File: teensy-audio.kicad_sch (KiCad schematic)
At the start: 50 parts, among them J1 AudioJack2, J10 Conn_01x05, J11 Conn_01x02, J12 Conn_01x04, J13 Conn_01x04, J2 AudioJack2, J3 Barrel_Jack, J4 Conn_02x06_Odd_Even, J5 Conn_02x08_Odd_Even, J6 Conn_02x05_Odd_Even, J7 Conn_01x04, J8 Conn_01x04, J9 Conn_02x05_Odd_Even, SW1 RotaryEncoder_Switch, SW2 SW_Push, SW3 SW_Push, SW4 SW_Push, SW5 SW_Push, U1 LM358, U2 LM7805_TO220, U3 Teensy4.0, U4 Teensy4.0_AudioShield_REVD

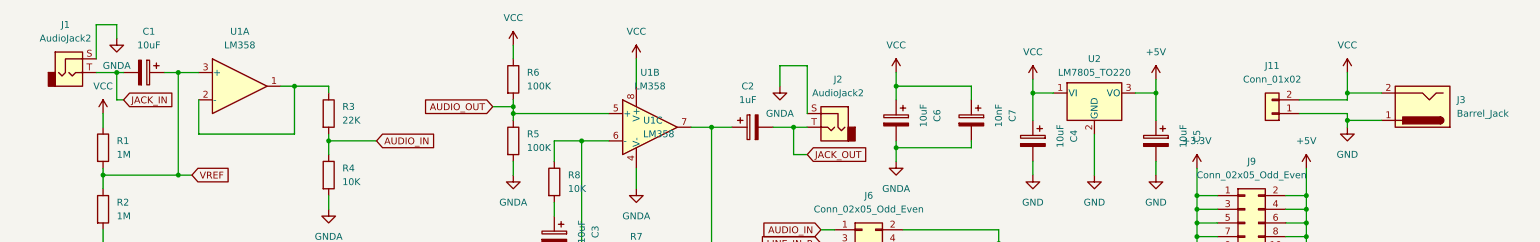
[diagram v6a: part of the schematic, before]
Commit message: corrected barrel plug
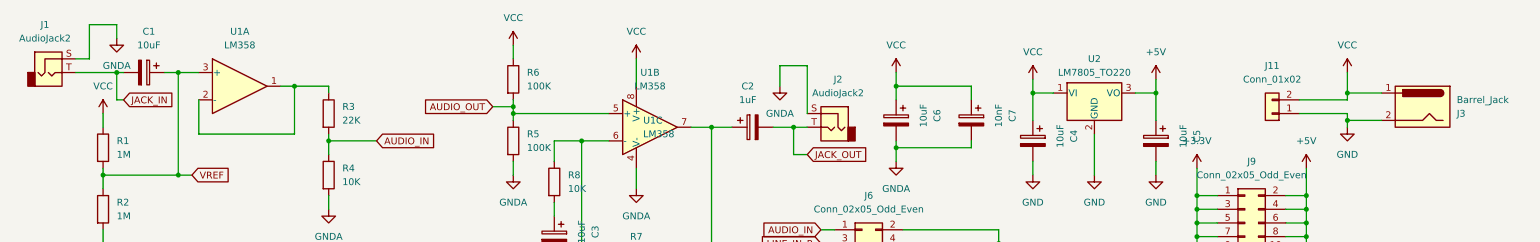
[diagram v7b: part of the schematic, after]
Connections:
- net GND: now also J3.2; no longer J3.1
- net VCC: now also J3.1; no longer J3.2
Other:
- moved on the sheet: J1, J3

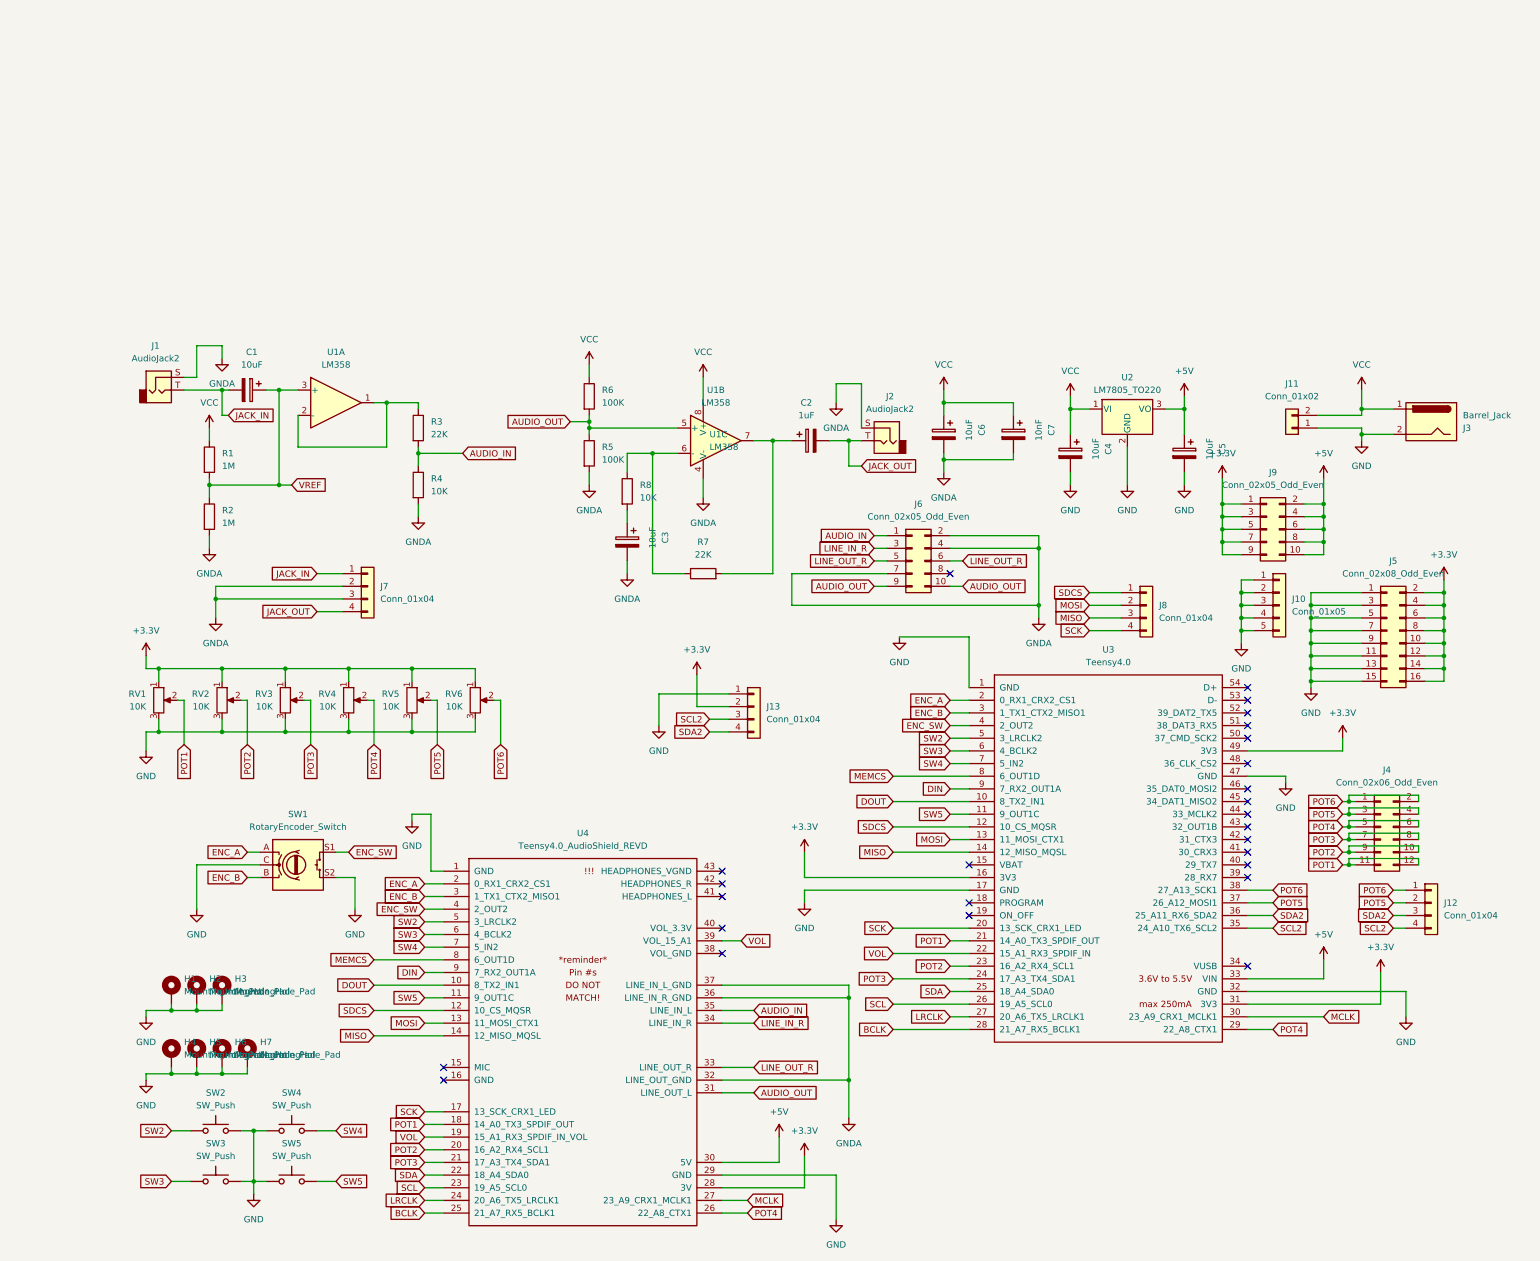
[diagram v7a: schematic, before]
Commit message: stereo input and output
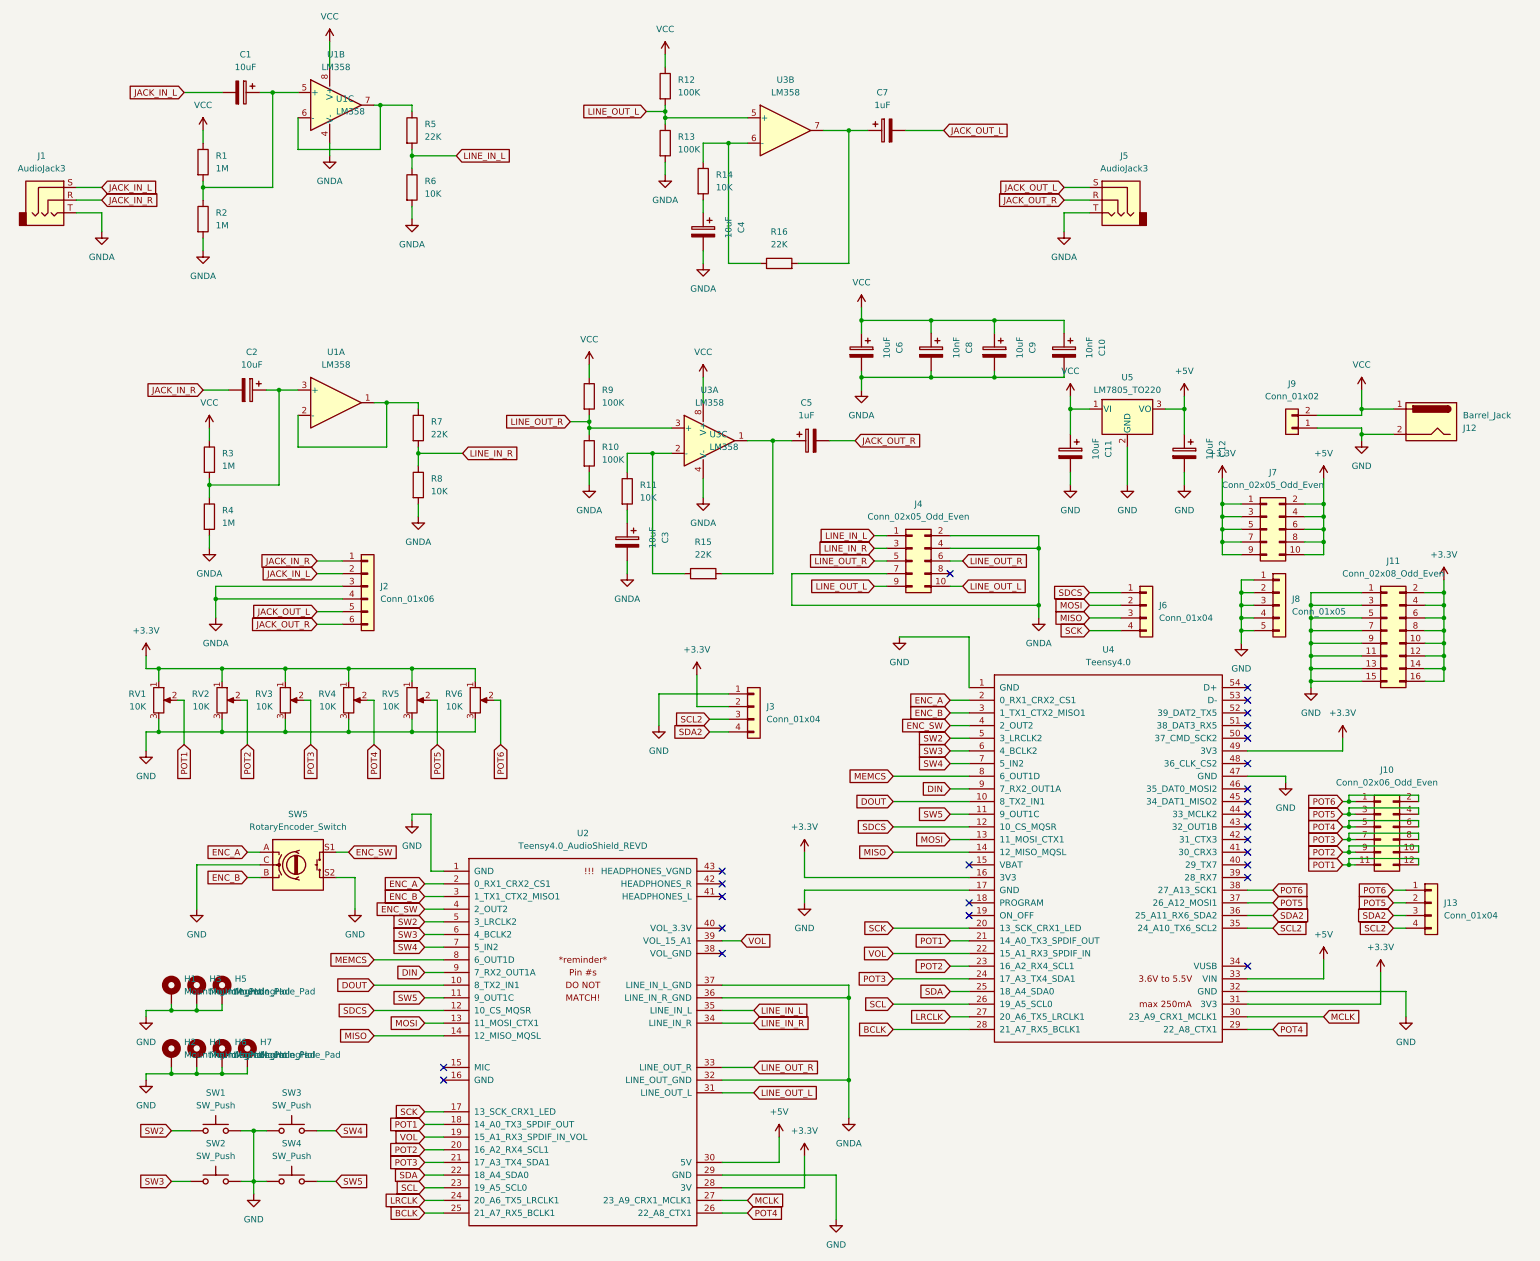
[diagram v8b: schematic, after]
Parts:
- removed J1, J2: AudioJack2, Connector_Audio:Jack_6.35mm_Neutrik_NMJ6HFD2-AU_Horizontal, symbol Connector:AudioJack2
- removed J7: Conn_01x04, Connector_PinHeader_2.54mm:PinHeader_1x04_P2.54mm_Vertical, symbol Connector_Generic:Conn_01x04
- added C1, C4, C9: 10uF, Capacitor_THT:CP_Radial_D4.0mm_P2.00mm, symbol Device:C_Polarized
- added C10: 10nF, Capacitor_THT:CP_Radial_D4.0mm_P2.00mm, symbol Device:C_Polarized
- added C7: 1uF, Capacitor_THT:CP_Radial_D4.0mm_P2.00mm, symbol Device:C_Polarized
- added J1, J5: AudioJack3, Connector_Audio:Jack_6.35mm_Neutrik_NMJ6HFD2-AU_Horizontal, symbol Connector-github:AudioJack3
- added J2: Conn_01x06, Connector_PinHeader_2.54mm:PinHeader_1x06_P2.54mm_Vertical, symbol Connector_Generic:Conn_01x06
- added R1, R2: 1M, Resistor_THT:R_Axial_DIN0207_L6.3mm_D2.5mm_P7.62mm_Horizontal, symbol Device:R
- added R12, R13: 100K, Resistor_THT:R_Axial_DIN0207_L6.3mm_D2.5mm_P7.62mm_Horizontal, symbol Device:R
- added R14, R6: 10K, Resistor_THT:R_Axial_DIN0207_L6.3mm_D2.5mm_P7.62mm_Horizontal, symbol Device:R
- added R16, R5: 22K, Resistor_THT:R_Axial_DIN0207_L6.3mm_D2.5mm_P7.62mm_Horizontal, symbol Device:R
- added U3: LM358, Package_DIP:DIP-8_W7.62mm_Socket, symbol Amplifier_Operational:LM358
- renumbered C4 to C11, C5 to C12, C1 to C2, C2 to C5, C7 to C8, H4 to H2, H2 to H3, H5 to H4, H3 to H5, J4 to J10, J5 to J11, J3 to J12, J12 to J13, J13 to J3, J6 to J4, J8 to J6, J9 to J7, J10 to J8, J11 to J9, R5 to R10, R8 to R11, R7 to R15, R1 to R3, R2 to R4, R3 to R7, R4 to R8, R6 to R9, SW2 to SW1, SW3 to SW2, SW4 to SW3, SW5 to SW4, SW1 to SW5, U4 to U2, U3 to U4, U2 to U5
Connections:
- net GNDA: now also C10.2, C4.2, C9.2, J1.T, J2.3 (Pin_3), J2.4 (Pin_4), J5.T, R13.2, R2.2, R6.2, U3.4 (V-)
- net LINE_IN_R: now also R7.2, R8.1
- net LINE_OUT_R: now also R10.1, R9.2, U3.3 (+)
- net VCC: now also C10.1, C9.1, R1.1, R12.1, U3.8 (V+)
- net at C5.1, R15.2: now also U3.1; no longer U1.7
- net at R11.1, R15.1: now also U3.2 (-); no longer U1.6 (-)
- net AUDIO_IN renamed LINE_IN_L
- net LINE_IN_L: now also R5.2, R6.1; no longer R7.2, R8.1
- net AUDIO_OUT renamed LINE_OUT_L
- net LINE_OUT_L: now also R12.2, R13.1, U3.5 (+); no longer R10.1, R9.2, U1.5 (+)
- net JACK_IN renamed JACK_IN_R
- net JACK_IN_R: now also J1.R, J2.1 (Pin_1)
- net JACK_OUT renamed JACK_OUT_R
- net JACK_OUT_R: now also J2.6 (Pin_6), J5.R
- net VREF: no longer names the net of C2.1, R3.2, R4.1, U1.3 (+)
- new net: C1.1, R1.2, R2.1, U1.5 (+)
- new net: R14.1, R16.1, U3.6 (-)
- new net: C4.1, R14.2
- new net: R5.1, U1.6 (-), U1.7
- new net: C7.1, R16.2, U3.7
- new net JACK_IN_L: C1.2, J1.S, J2.2 (Pin_2)
- new net JACK_OUT_L: C7.2, J2.5 (Pin_5), J5.S
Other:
- moved on the sheet: C6, C8, U1B, U1C
